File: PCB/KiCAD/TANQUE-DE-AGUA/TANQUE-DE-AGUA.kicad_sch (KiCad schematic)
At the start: 46 parts

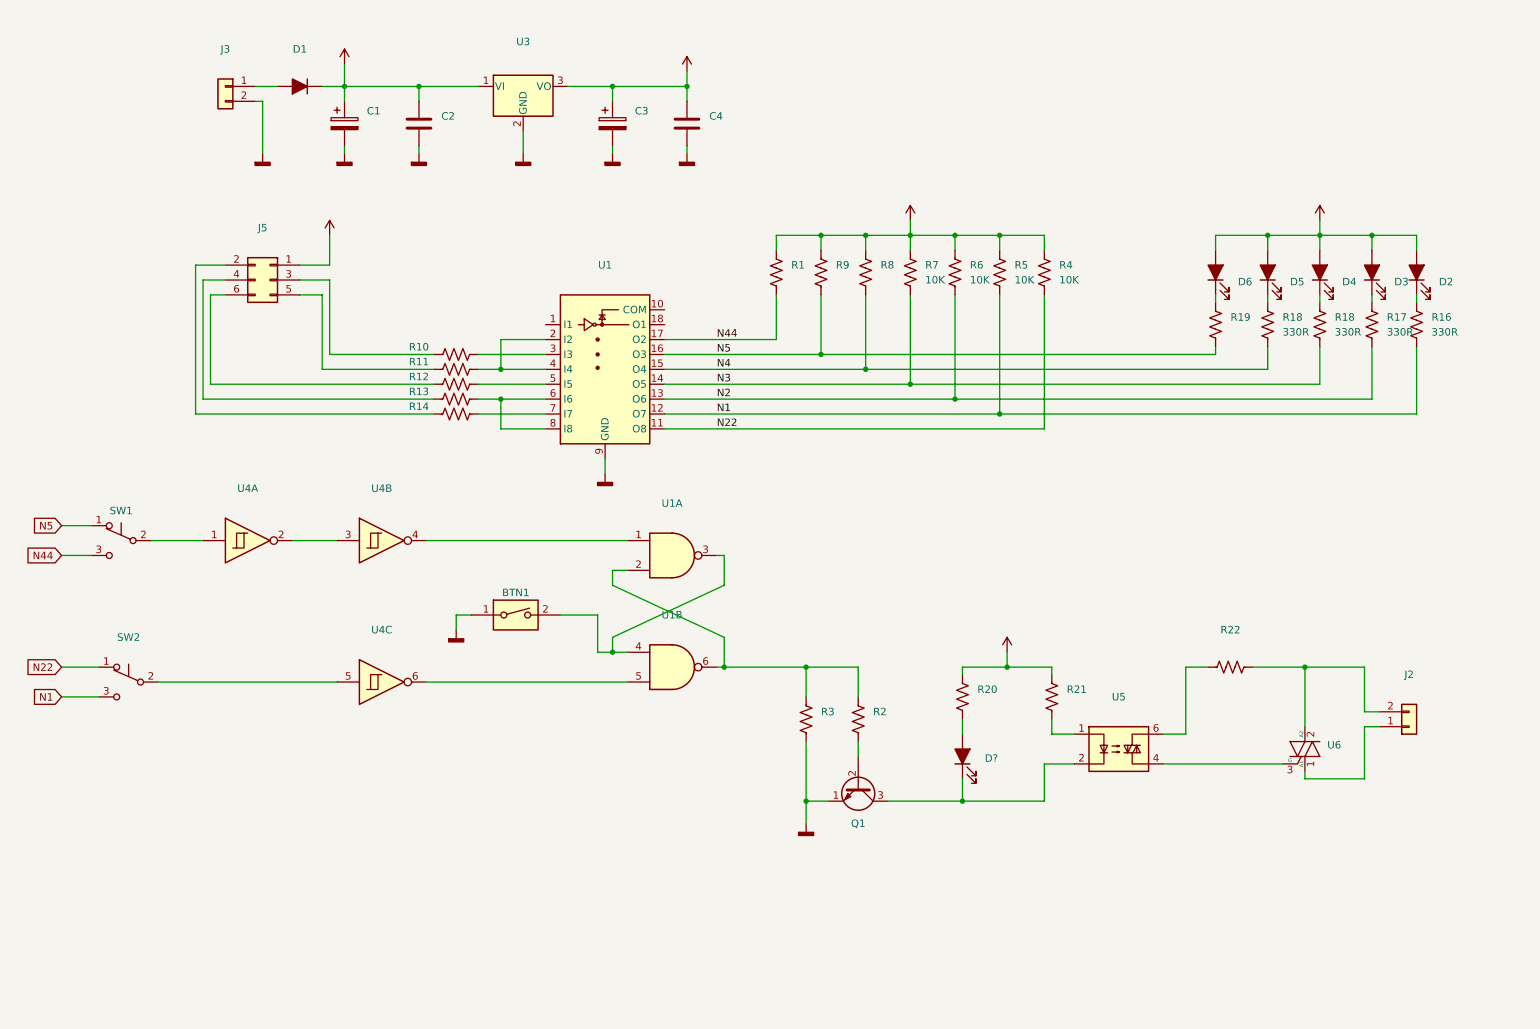
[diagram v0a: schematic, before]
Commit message: En caso de bloquedo de sensor, forzar apagado
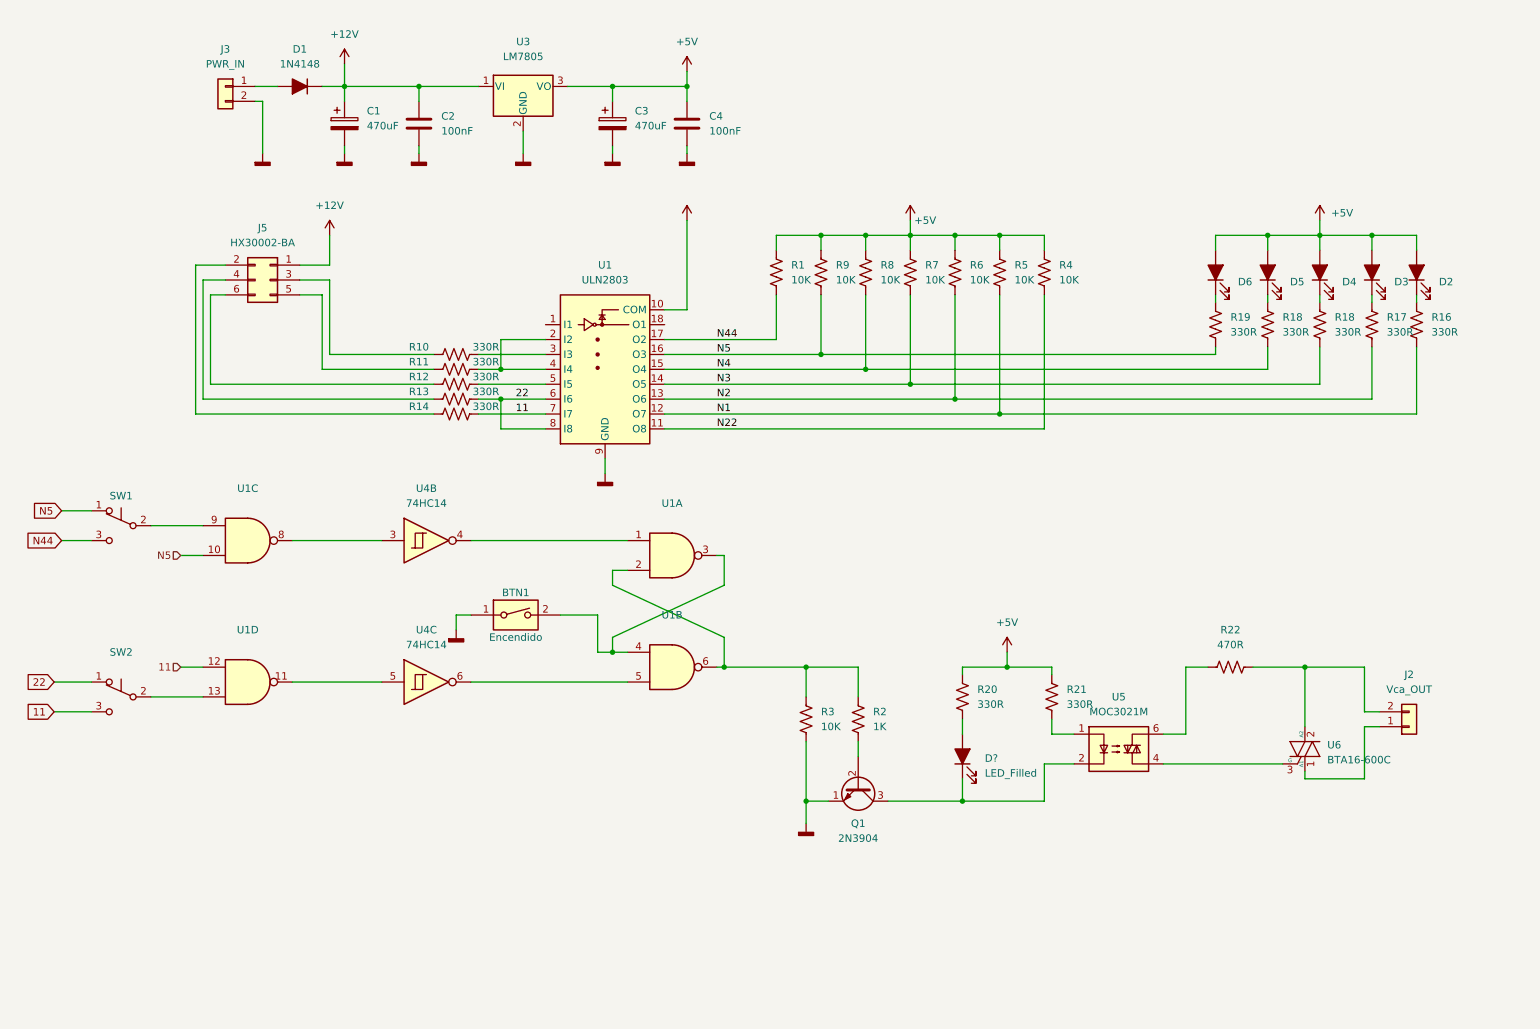
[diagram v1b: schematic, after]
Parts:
- removed unit 1 of U4
- added unit 4 of U1
- added unit 3 of U1
- BTN1: value (none) -> Encendido
- C1, C3: value (none) -> 470uF
- C2, C4: value (none) -> 100nF
- D1: value (none) -> 1N4148
- D6: value (none) -> LED
- D?: value (none) -> LED_Filled
- J2: value (none) -> Vca_OUT
- J3: value (none) -> PWR_IN
- J5: value (none) -> HX30002-BA
- Q1: value (none) -> 2N3904; footprint (none) -> Package_TO_SOT_THT:TO-92_Inline
- R1, R3, R8, R9: value (none) -> 10K
- R10, R11, R12, R13, R14, R19, R20, R21: value (none) -> 330R
- R2: value (none) -> 1K
- R22: value (none) -> 470R
- SW1, SW2: value (none) -> SW_Push_SPDT
- U1: value (none) -> ULN2803
- U3: value (none) -> LM7805; footprint (none) -> Package_TO_SOT_THT:TO-220-3_Vertical
- U4: value (none) -> 74HC14
- U5: value (none) -> MOC3021M
- U6: value (none) -> BTA16-600C; footprint (none) -> Package_TO_SOT_THT:TO-220-3_Vertical
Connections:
- net +5V: now also U1.10 (COM)
- net N1: no longer SW2.3 (C)
- net N22: no longer SW2.1 (A)
- net N5: now also U1.10
- net 22: now reaches R13.2, U1.6 (I6), U1.8 (I8)
- net 22: now also SW2.1 (A)
- net 11: now reaches R14.2, U1.7 (I7)
- net 11: now also SW2.3 (C), U1.12
- net at SW1.2 (B): now also U1.9
- net at U4.3: now also U1.8
- net at U4.5: now also U1.11; no longer SW2.2 (B)
- new net: SW2.2 (B), U1.13
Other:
- moved on the sheet: SW1, SW2, U4B, U4C

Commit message: Actualizacion del diagrama y primer bosquejo del PCB hecho en KiCAD
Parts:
- removed J3: PWR_IN, symbol Connector_Generic:Conn_01x02
- removed R1, R4, R5, R6, R7, R8, R9: 10K, symbol Device:R_US
- removed U1: ULN2803, symbol Transistor_Array:ULN2803A
- added J3: (no value), symbol Connector:Barrel_Jack_Switch
- added unit 5 of U1
- added U2: ULN2003, Package_DIP:DIP-16_W7.62mm_LongPads, symbol Transistor_Array:ULN2003
- added unit 7 of U4
- BTN1: footprint (none) -> Button_Switch_THT:SW_PUSH_6mm_H4.3mm
- C1, C3: footprint (none) -> Capacitor_THT:CP_Radial_D6.3mm_P2.50mm
- C2, C4: footprint (none) -> Capacitor_THT:C_Disc_D7.5mm_W2.5mm_P5.00mm
- D1: footprint (none) -> Diode_THT:D_A-405_P7.62mm_Horizontal
- D2: value LED -> 20%; footprint (none) -> LED_THT:LED_D3.0mm
- D3: value LED -> 40%; footprint (none) -> LED_THT:LED_D3.0mm
- D4: value LED -> 60%; footprint (none) -> LED_THT:LED_D3.0mm
- D5: value LED -> 80%; footprint (none) -> LED_THT:LED_D3.0mm
- D6: value LED -> 100%; footprint (none) -> LED_THT:LED_D3.0mm
- D7: renamed from D?; value LED_Filled -> ENCENDIDO; footprint (none) -> LED_THT:LED_D3.0mm_IRGrey
- J2: footprint (none) -> TerminalBlock_Phoenix:TerminalBlock_Phoenix_MPT-0,5-2-2.54_1x02_P2.54mm_Horizontal
- J5: footprint (none) -> Connector_PinSocket_2.54mm:PinSocket_2x03_P2.54mm_Vertical
- R10, R11, R12, R13, R14: value 330R -> 1K; footprint (none) -> Resistor_THT:R_Axial_DIN0207_L6.3mm_D2.5mm_P10.16mm_Horizontal
- R15: renamed from R16; footprint (none) -> Resistor_THT:R_Axial_DIN0207_L6.3mm_D2.5mm_P10.16mm_Horizontal
- R16: renamed from R17; footprint (none) -> Resistor_THT:R_Axial_DIN0207_L6.3mm_D2.5mm_P10.16mm_Horizontal
- R17: renamed from R18; footprint (none) -> Resistor_THT:R_Axial_DIN0207_L6.3mm_D2.5mm_P10.16mm_Horizontal
- R18, R19, R2, R20, R21, R22, R3: footprint (none) -> Resistor_THT:R_Axial_DIN0207_L6.3mm_D2.5mm_P10.16mm_Horizontal
- SW1: value SW_Push_SPDT -> Nivel MAX; footprint (none) -> Connector_PinHeader_2.54mm:PinHeader_1x03_P2.54mm_Vertical
- SW2: value SW_Push_SPDT -> Nivel Min; footprint (none) -> Connector_PinHeader_2.54mm:PinHeader_1x03_P2.54mm_Vertical
- U1: value (none) -> 74HC00; footprint (none) -> Package_DIP:DIP-14_W7.62mm_LongPads
- U4: footprint (none) -> Package_DIP:DIP-14_W7.62mm_LongPads
- U5: footprint (none) -> Package_DIP:DIP-6_W7.62mm_LongPads
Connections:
- net N2 is gone; now on an unnamed net: R16.1
- net N4 is gone; now on an unnamed net: R18.1
- net +12V: no longer J5.1 (Pin_1)
- net +5V: now also J5.1 (Pin_1), U1.14 (VCC), U2.9 (COM), U4.14 (VCC)
- net 11: now also J5.2 (Pin_2), R10.1, U1.4, U2.6 (I6); no longer R14.2, U1.12
- net 22: now also J5.4 (Pin_4), R11.1, U2.5 (I5), U2.7 (I7); no longer R13.2
- net GNDD: now also R10.2, R11.2, R12.2, R13.2, R14.2, J3.2, J3.3, U1.7 (GND), U2.8 (GND), U4.7 (GND)
- net N1: now also R15.2, U2.11 (O6); no longer R15.1
- net N22: now also R16.2, U2.10 (O7), U2.12 (O5)
- net N3: now also R17.2, U2.13 (O4); no longer R17.1
- net N44: now also R18.2, U2.14 (O3), U2.16 (O1)
- net N5: now also R19.2, U1.2, U2.15 (O2); no longer R19.1, U1.10
- net at D1.2 (A): now also J3.1
- net at D2.1 (K): now also R15.1; no longer R15.2
- net at R13.1: now also J5.5 (Pin_5), U2.1 (I1), U2.3 (I3); no longer J5.4 (Pin_4)
- net at SW2.2 (B): now also U1.5; no longer U1.13
- net at J5.3 (Pin_3): now also R14.1, U2.2 (I2); no longer R10.1
- net at SW1.2 (B): now also U1.1; no longer U1.9
- net at R2.1, R3.1: now also U1.10, U1.11; no longer U1.2, U1.6
- net at D3.1 (K): no longer R16.2
- net at D4.1 (K): now also R17.1; no longer R17.2
- net at D5.1 (K): no longer R18.2
- net at D6.1 (K): now also R19.1; no longer R19.2
- net at J5.6 (Pin_6), R12.1: now also U2.4 (I4)
- new net: U1.6, U4.13
- new net: BTN1.2, U1.12, U1.8
- new net: U1.3, U4.11
- new net: U1.9, U4.10
- new net: U1.13, U4.12
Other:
- moved on the sheet: C1, C2, C3, C4, D1, D2, D3, D4, D5, D6, J5, R15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
